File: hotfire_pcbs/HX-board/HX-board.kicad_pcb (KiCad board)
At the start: 2 copper layers, 101.6 x 88.5 mm, 55 parts, among them J1 Testpoints, J2 PCIE-LP-01-01-F-DV-A-TR, J3 DB15_Female, J4 Testpoints, J5 DB15_Female, J6 Testpoints, U1 HX711_Breakout, U2 HX711_Breakout, U3 HX711_Breakout, U4 HX711_Breakout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

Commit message: Finished wiring HX. Need review + silkscreen.
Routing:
- net +5V: track 0.00 -> 189.7 mm
- net /HX_CLK: track 0.00 -> 173.4 mm, vias 0 -> 2
- net /PT4_E+: track 0.00 -> 147.3 mm, vias 0 -> 1
- net /PT4_A+: track 0.00 -> 142.4 mm
- net /PT4_E-: track 0.00 -> 135.8 mm
- net /PT4_A-: track 0.00 -> 133.7 mm
- net /PT5_E+: track 2.77 -> 111.8 mm, vias 0 -> 1
- net /PT5_A+: track 0.00 -> 107.9 mm
- net /PCIe_3: track 0.00 -> 99.1 mm, vias 0 -> 2
- net /PT5_E-: track 6.71 -> 100.4 mm
- net /PCIe_8: track 0.00 -> 90.4 mm
- net /PT5_A-: track 10.5 -> 98.8 mm
- net /PCIe_5: track 0.00 -> 86.4 mm, vias 0 -> 2
- net /PCIe_2: track 0.00 -> 70.6 mm, vias 0 -> 1
- net /PT3_E+: track 2.57 -> 72.6 mm, vias 0 -> 1
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
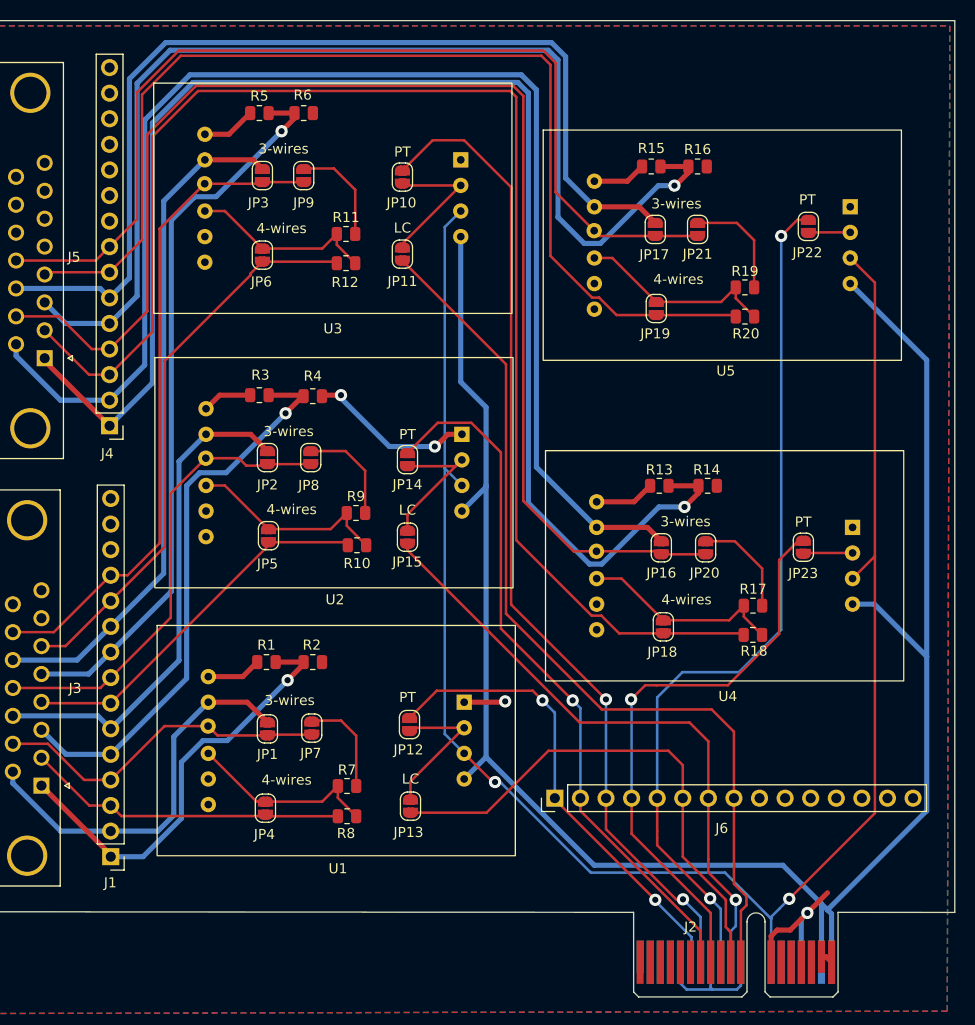
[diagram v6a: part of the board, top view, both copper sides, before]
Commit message: Added silkscreen.
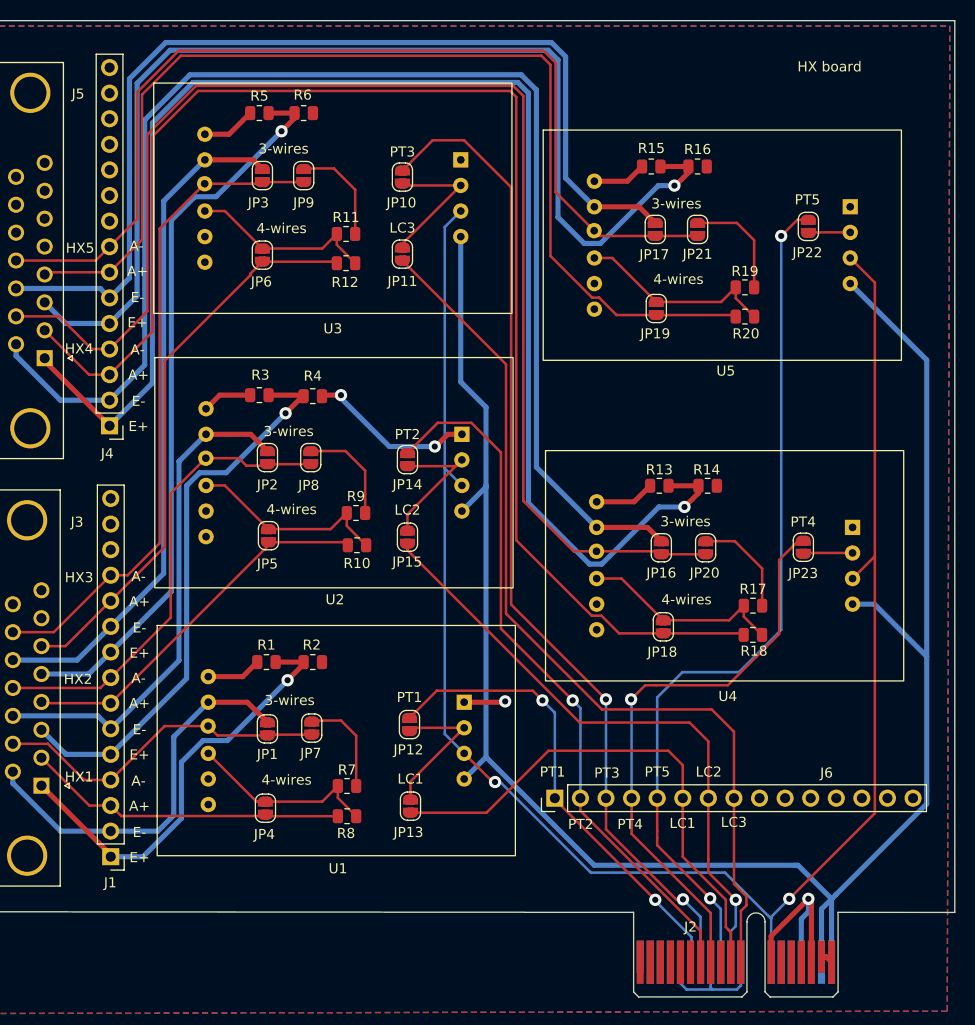
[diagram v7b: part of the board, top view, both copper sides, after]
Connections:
- net /HX_DT_1 renamed /HX1_DT
- net /HX_DT_2 renamed /HX2_DT
- net /HX_DT_3 renamed /HX3_DT
- net /HX_DT_4 renamed /HX4_DT
- net /HX_DT_5 renamed /HX5_DT
- net /PCIe_1 renamed /PT1_DT
- net /PCIe_2 renamed /PT2_DT
- net /PCIe_3 renamed /PT3_DT
- net /PCIe_4 renamed /PT4_DT
- net /PCIe_5 renamed /PT5_DT
- net /PCIe_6 renamed /LC1_DT
- net /PCIe_7 renamed /LC2_DT
- net /PCIe_8 renamed /LC3_DT
- net /PT1_A+ renamed /HX1_A+
- net /PT1_A- renamed /HX1_A-
- net /PT1_E+ renamed /HX1_E+
- net /PT1_E- renamed /HX1_E-
- net /PT2_A+ renamed /HX2_A+
- net /PT2_A- renamed /HX2_A-
- net /PT2_E+ renamed /HX2_E+
- net /PT2_E- renamed /HX2_E-
- net /PT3_A+ renamed /HX3_A+
- net /PT3_A- renamed /HX3_A-
- net /PT3_E+ renamed /HX3_E+
- net /PT3_E- renamed /HX3_E-
- net /PT4_A+ renamed /HX4_A+
- net /PT4_A- renamed /HX4_A-
- net /PT4_E+ renamed /HX4_E+
- net /PT4_E- renamed /HX4_E-
- net /PT5_A+ renamed /HX5_A+
- net /PT5_A- renamed /HX5_A-
- net /PT5_E+ renamed /HX5_E+
- net /PT5_E- renamed /HX5_E-
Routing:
- net GND: track 49.6 -> 55.3 mm
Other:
- board text added: "A+"
- board text added: "A-"
- board text added: "E+"
- board text added: "E-"
- board text added: "HX board"
- board text added: "HX1"
- board text added: "HX2"
- board text added: "HX3"
- board text added: "HX4"
- board text added: "HX5"
- board text added: "LC1"
- board text added: "LC2"
- board text added: "LC3"
- board text added: "PT1"
- board text added: "PT2"
- board text added: "PT3"
- board text added: "PT4"
- board text added: "PT5"
- board text removed: "LC"
- board text removed: "PT"
